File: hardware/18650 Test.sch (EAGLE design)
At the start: 3 parts

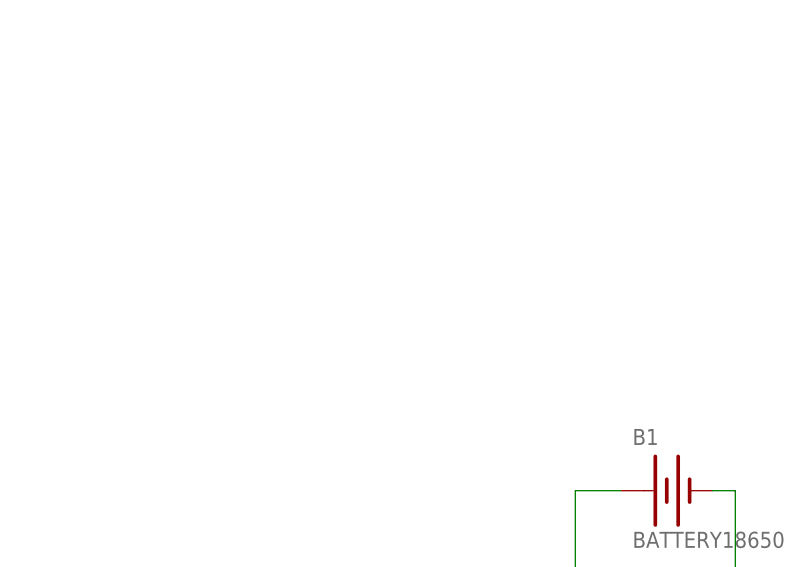
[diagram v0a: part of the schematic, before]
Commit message: v2 with Charge/Discharge MOSFET control and cell balancing
Many changes. Added large MOSFETs and pack interface circuitry. Added
small MOSFETs for individual cell balancing/charging. Corrected
Thermistor pull down error. All FPs pass 1:1 check.
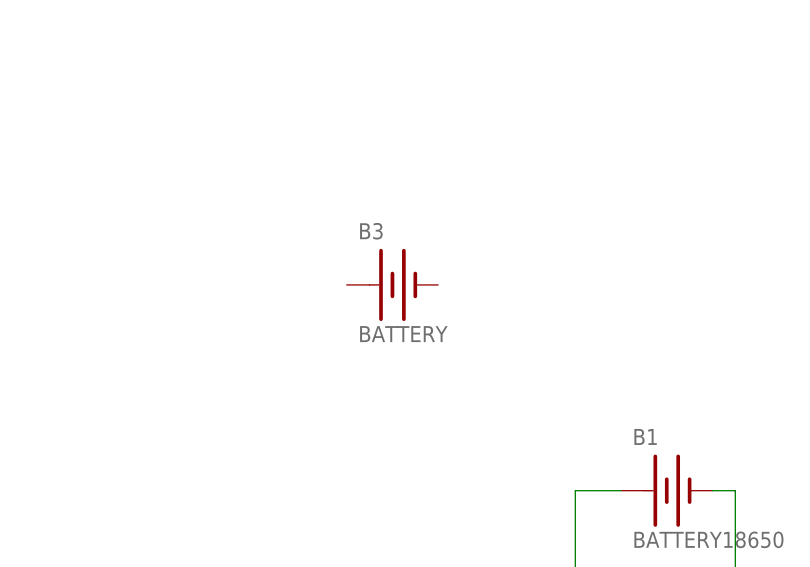
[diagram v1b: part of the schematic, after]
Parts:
- added B3: BATTERY, bq769x0:BATTERY
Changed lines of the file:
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@@
 <part name="B1" library="bq769x0" deviceset="BATTERY" device="18650"/>
 <part name="JP1" library="SparkFun-Connectors" deviceset="M02" device="PTH"/>
+<part name="B3" library="bq769x0" deviceset="BATTERY" device=""/>
 </parts>
 <sheets>
@@
 <instance part="B1" gate="B1" x="93.98" y="63.5"/>
 <instance part="JP1" gate="G$1" x="93.98" y="35.56" rot="R90"/>
+<instance part="B3" gate="B1" x="63.5" y="86.36"/>
 </instances>
 <busses>
